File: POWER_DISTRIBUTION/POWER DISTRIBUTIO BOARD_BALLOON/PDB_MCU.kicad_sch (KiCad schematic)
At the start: 15 parts, among them U6 ESP32-WROOM-32E

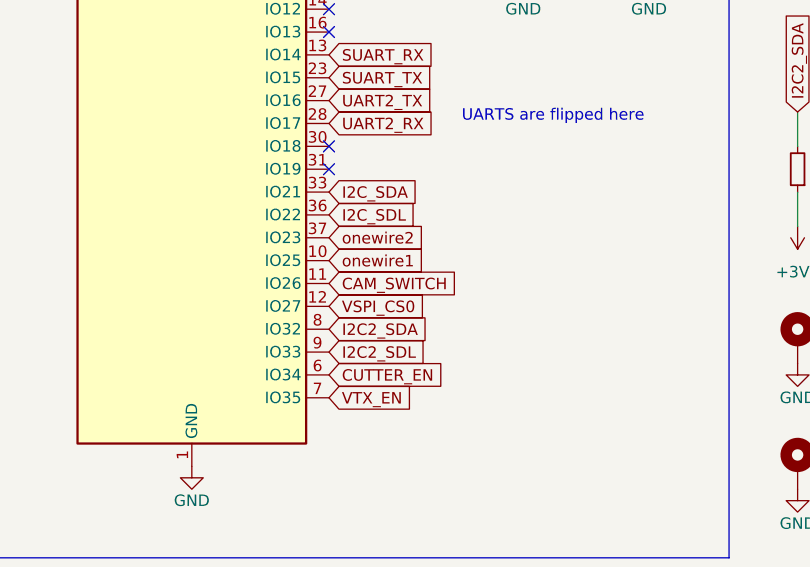
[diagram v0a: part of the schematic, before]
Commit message: added some global labels
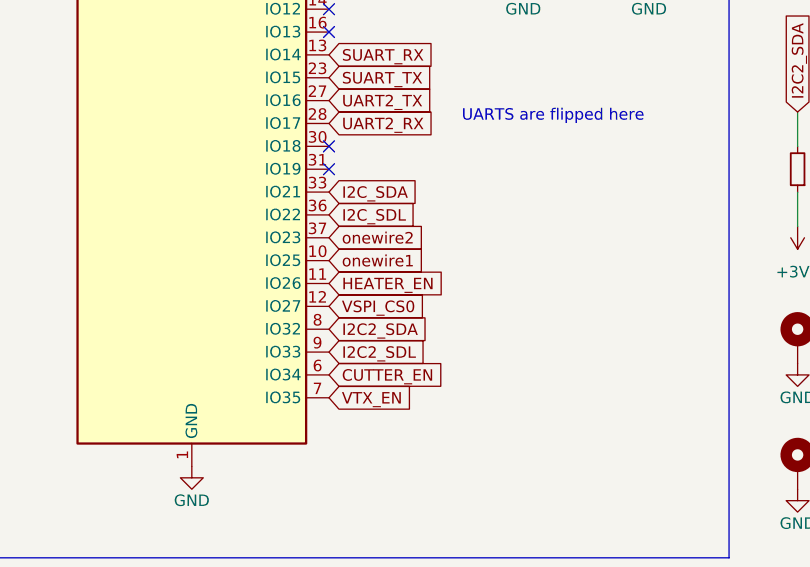
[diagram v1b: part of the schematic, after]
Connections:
- net CAM_SWITCH renamed HEATER_EN
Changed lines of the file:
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@@
 		)
 	)
-	(global_label "CAM_SWITCH"
+	(global_label "HEATER_EN"
 		(shape input)
 		(at 73.66 99.06 0)
@@
 		)
 		(property "Intersheetrefs" "${INTERSHEET_REFS}"
-			(at 88.2566 99.06 0)
+			(at 87.047 99.06 0)
 			(effects
 				(font

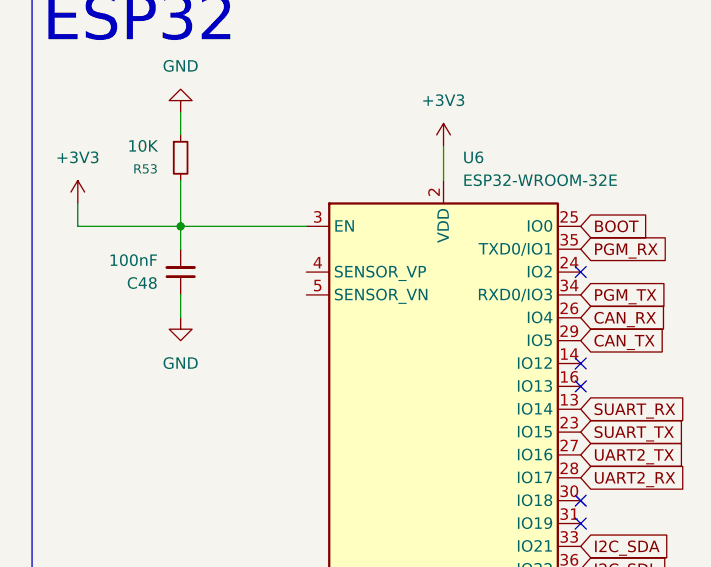
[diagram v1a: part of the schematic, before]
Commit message: almost finished wiring
btw for the i2c bus idk if it was meant to be SCL instead of SDL , there is alr an SDA line but i assume so
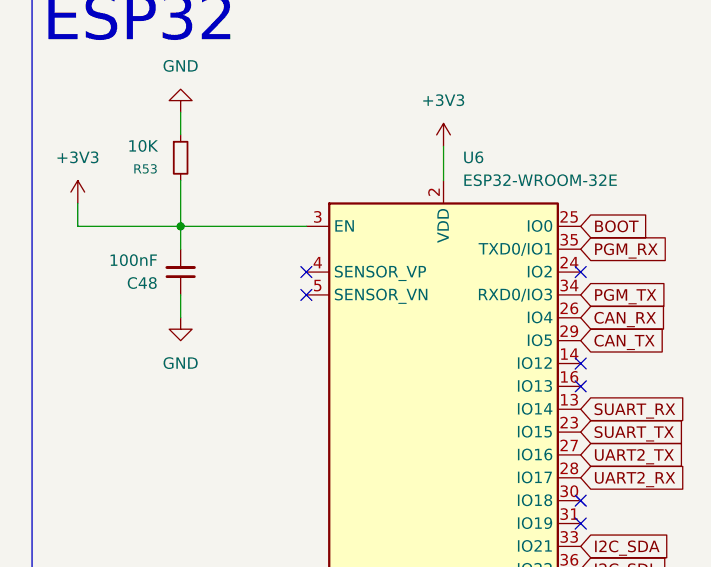
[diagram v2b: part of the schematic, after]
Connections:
- no-connect marks 5 -> 7
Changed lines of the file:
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@@
+	)
+	(no_connect
+		(at 43.18 60.96)
 	)
 	(no_connect
@@
 	)
 	(no_connect
+		(at 43.18 58.42)
+	)
+	(no_connect
